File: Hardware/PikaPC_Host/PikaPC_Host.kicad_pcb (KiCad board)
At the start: 4 copper layers, 101.6 x 101.6 mm, 225 parts, among them J1 DE9_Pins_MountingHoles, J2 DIN41612_03x32_C_Split, J3 Conn_01x03, SW1 SW_Push, U1 PPC403GA, U10 74ALVC164245, U11 74ALVC164245, U12 74ALVC164245, U2 ATF1508AS, U3 MCP120-315GI/TO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

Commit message: Un-assign main bus pins 22 & 23
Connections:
- J2 pad b22: GND -> unconnected-(J2B-Pin_b22-Padb22)
- J2 pad b23: GND -> unconnected-(J2B-Pin_b23-Padb23)

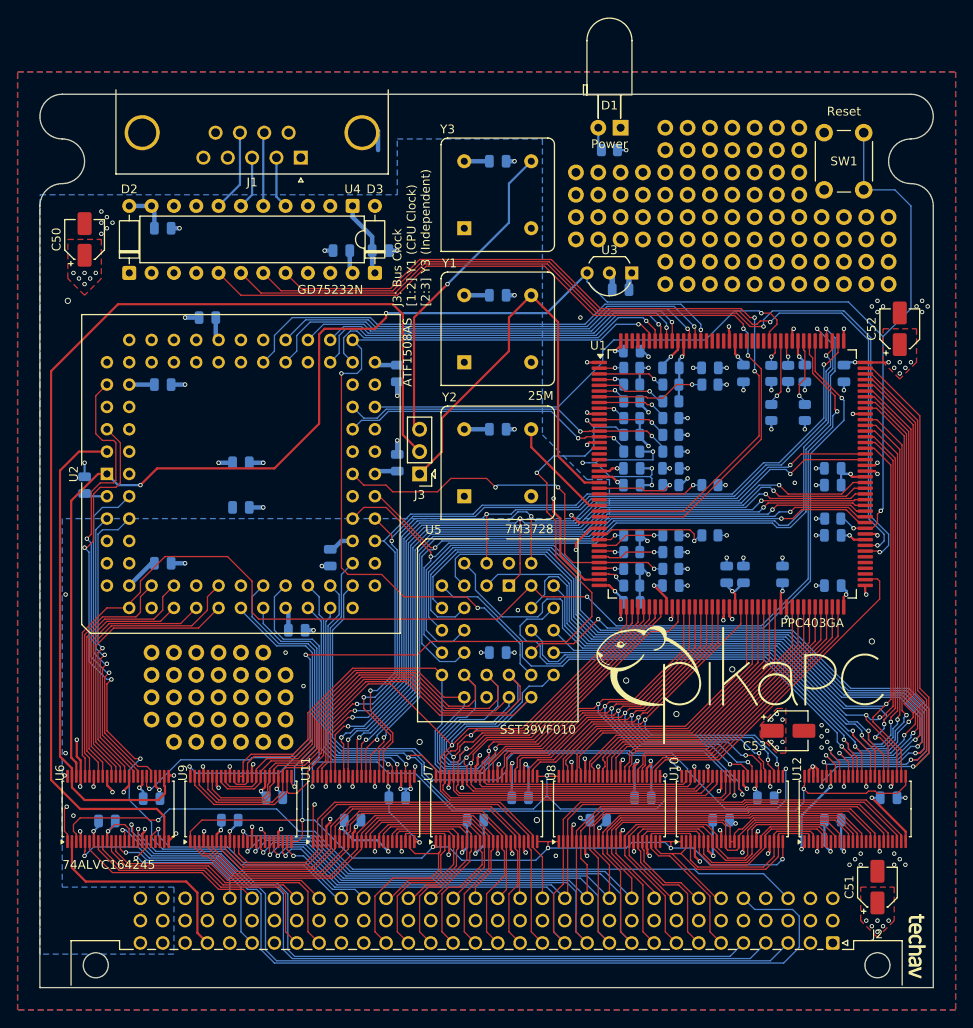
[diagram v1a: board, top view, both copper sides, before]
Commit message: Annotate & prep for output - Host & KBC
add gerber output to gitignore
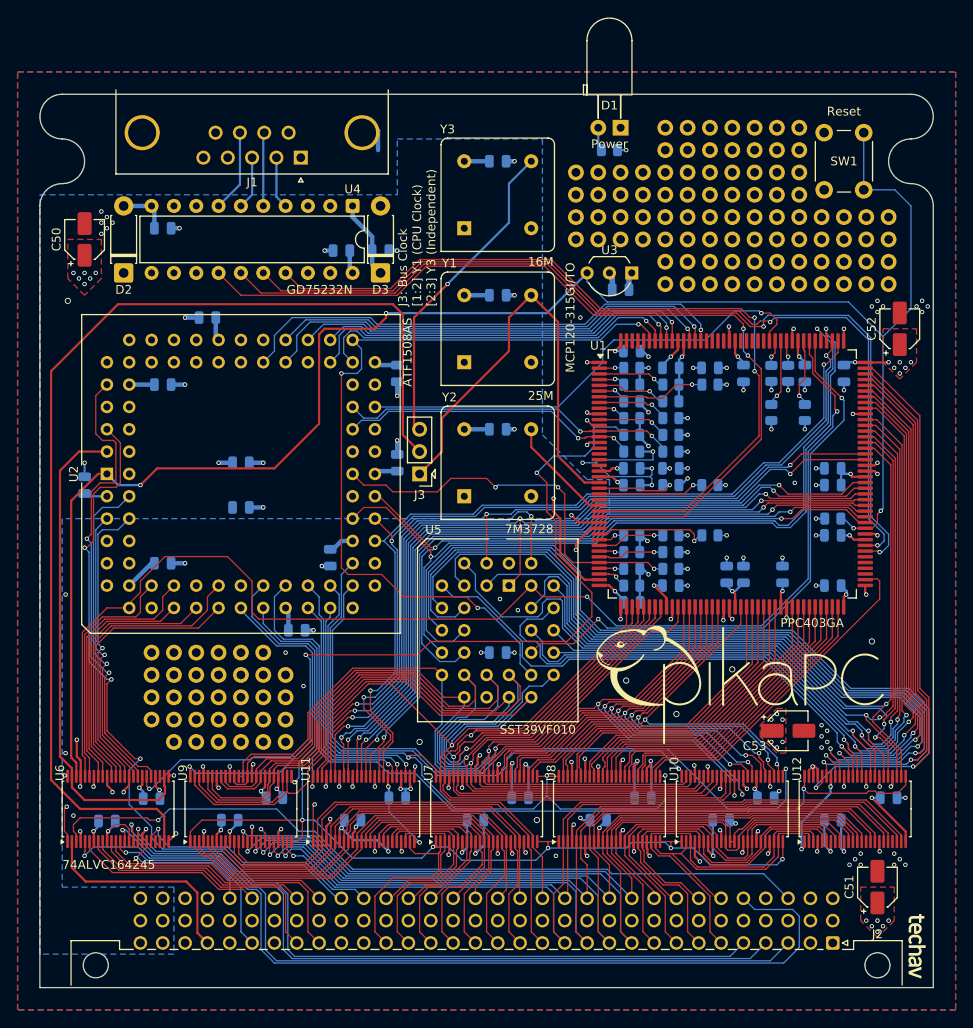
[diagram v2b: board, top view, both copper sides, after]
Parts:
- D2, D3: value 1N4148 -> 1N4004; footprint Diode_THT:D_DO-35_SOD27_P7.62mm_Horizontal -> Diode_THT:D_DO-41_SOD81_P7.62mm_Horizontal
- Y3: value 25M -> 16M
- moved D2 0.64 mm to (85.7, 71.1)
- moved D3 0.64 mm to (114.9, 71.1)
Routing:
- net /Main Bus/~{BEN-8-0}: track 67.1 -> 65.9 mm
- net /Main Bus/~{BEN-8-1}: track 30.5 -> 29.5 mm
- net /Main Bus/A29: track 150.7 -> 151.7 mm
- net /Serial/COM_-12V: track 5.21 -> 5.85 mm
- net /CPU Bus/D15: track 52.8 -> 52.2 mm
